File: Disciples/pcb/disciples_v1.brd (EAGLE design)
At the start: 19 x 108.4 mm, 101 parts, among them IC1 OPA1641, IC2 LM324PW, IC3 LM324PW, IC4 TL072D, IC5 LM324PW, IC6 LM4040B10, J1 PJ301_THONKICONN6, J10 PJ301_THONKICONN6, J11 PJ301_THONKICONN6, J2 PJ301_THONKICONN6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

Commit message: Restructure, fixed LEDs
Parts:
- added LED5: WP710A10GD, led:LED3MM
- added R17: 10k, rcl:R0402
- LED4: value WP-710A10GD -> WP710A10SEC/J3
- moved LED2 200.3 mm to (1.27, -447.0)
- moved R9 200.3 mm to (0.64, -442.3)
- moved R10 191.2 mm to (0.64, -461.3)
- moved LED3 191.1 mm to (1.27, -466.1)
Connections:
- new net N$46: IC5.14, LED2.A
- new net N$48: IC5.13, LED2.K, R9.1
- net COMP: no longer IC5.12
- net GND: now also R17.2
- net LOWPASS: now also IC5.12
- net N$17: now also LED3.K, R10.2; no longer LED2.K, R9.1
- net N$30: now also LED3.A; no longer LED2.A
- net N$37: now also LED5.K, R17.1; no longer IC5.13, LED3.K, R10.2
- net N$38: now also LED5.A; no longer IC5.14, LED3.A
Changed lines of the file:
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@@
 <attribute name="VALUE" x="0.3175" y="-149.86" size="1.27" layer="27"/>
 </element>
-<element name="LED4" library="led" package="LED3MM" value="WP-710A10GD" x="1.5875" y="-187.0075" smashed="yes">
+<element name="LED4" library="led" package="LED3MM" value="WP710A10SEC/J3" x="1.5875" y="-187.0075" smashed="yes">
 <attribute name="NAME" x="3.4925" y="-186.6265" size="1.27" layer="25" ratio="10"/>
 <attribute name="VALUE" x="3.4925" y="-188.6585" size="1.27" layer="27" ratio="10"/>
@@
 <attribute name="VALUE" x="5.08" y="-230.1875" size="1.27" layer="27"/>
 </element>
-<element name="R9" library="rcl" package="R0402" value="20k" x="0.635" y="-241.935" smashed="yes">
-<attribute name="NAME" x="0" y="-241.3" size="1.27" layer="25"/>
-<attribute name="VALUE" x="0" y="-243.84" size="1.27" layer="27"/>
-</element>
-<element name="LED2" library="led" package="LED3MM" value="AOL-3MWY4" x="1.27" y="-246.6975" smashed="yes">
-<attribute name="NAME" x="3.175" y="-246.3165" size="1.27" layer="25" ratio="10"/>
-<attribute name="VALUE" x="3.175" y="-248.3485" size="1.27" layer="27" ratio="10"/>
-</element>
-<element name="LED3" library="led" package="LED3MM" value="WP710A10SEC/J4" x="1.27" y="-274.955" smashed="yes">
-<attribute name="NAME" x="3.175" y="-274.574" size="1.27" layer="25" ratio="10"/>
-<attribute name="VALUE" x="3.175" y="-276.606" size="1.27" layer="27" ratio="10"/>
-</element>
-<element name="R10" library="rcl" package="R0402" value="10k" x="5.3975" y="-270.1925" smashed="yes">
-<attribute name="NAME" x="4.7625" y="-269.5575" size="1.27" layer="25"/>
-<attribute name="VALUE" x="4.7625" y="-272.0975" size="1.27" layer="27"/>
-</element>
 <element name="C1" library="rcl" package="C1206" value="22u" x="1.905" y="-280.3525" smashed="yes">
 <attribute name="NAME" x="0.635" y="-279.0825" size="1.27" layer="25"/>
@@
 <attribute name="NAME" x="0" y="-436.5625" size="1.27" layer="25"/>
 <attribute name="VALUE" x="0" y="-439.1025" size="1.27" layer="27"/>
+</element>
+<element name="R9" library="rcl" package="R0402" value="20k" x="0.635" y="-442.2775" smashed="yes">
+<attribute name="NAME" x="0" y="-441.6425" size="1.27" layer="25"/>
+<attribute name="VALUE" x="0" y="-444.1825" size="1.27" layer="27"/>
+</element>
+<element name="LED2" library="led" package="LED3MM" value="AOL-3MWY4" x="1.27" y="-447.04" smashed="yes">
+<attribute name="NAME" x="3.175" y="-446.659" size="1.27" layer="25" ratio="10"/>
+<attribute name="VALUE" x="3.175" y="-448.691" size="1.27" layer="27" ratio="10"/>
+</element>
+<element name="LED3" library="led" package="LED3MM" value="WP710A10SEC/J4" x="1.27" y="-466.09" smashed="yes">
+<attribute name="NAME" x="3.175" y="-465.709" size="1.27" layer="25" ratio="10"/>
+<attribute name="VALUE" x="3.175" y="-467.741" size="1.27" layer="27" ratio="10"/>
+</element>
+<element name="R10" library="rcl" package="R0402" value="10k" x="0.635" y="-461.3275" smashed="yes">
+<attribute name="NAME" x="0" y="-460.6925" size="1.27" layer="25"/>
+<attribute name="VALUE" x="0" y="-463.2325" size="1.27" layer="27"/>
+</element>
+<element name="R17" library="rcl" package="R0402" value="10k" x="0.635" y="-470.8525" smashed="yes">
+<attribute name="NAME" x="0" y="-470.2175" size="1.27" layer="25"/>
+<attribute name="VALUE" x="0" y="-472.7575" size="1.27" layer="27"/>
+</element>
+<element name="LED5" library="led" package="LED3MM" value="WP710A10GD" x="1.27" y="-475.615" smashed="yes">
+<attribute name="NAME" x="3.175" y="-475.234" size="1.27" layer="25" ratio="10"/>
+<attribute name="VALUE" x="3.175" y="-477.266" size="1.27" layer="27" ratio="10"/>
 </element>
 </elements>
@@
 <contactref element="C14" pad="2"/>
 <contactref element="IC6" pad="2"/>
-<contactref element="R9" pad="2"/>
-<contactref element="R10" pad="1"/>
 <contactref element="C1" pad="2"/>
 <contactref element="C2" pad="1"/>
@@
 <contactref element="C20" pad="1"/>
 <contactref element="C21" pad="2"/>
-<wire x1="4.7475" y1="-270.1925" x2="1.285" y2="-241.935" width="0" layer="19" extent="1-1"/>
-<wire x1="3.305" y1="-280.3525" x2="4.7475" y2="-270.1925" width="0" layer="19" extent="1-1"/>
-<wire x1="0.505" y1="-286.7025" x2="3.305" y2="-280.3525" width="0" layer="19" extent="1-1"/>
-<wire x1="1.285" y1="-297.4975" x2="0.505" y2="-286.7025" width="0" layer="19" extent="1-1"/>
-<wire x1="-0.015" y1="-302.5775" x2="1.285" y2="-297.4975" width="0" layer="19" extent="1-1"/>
-<wire x1="3.81" y1="-344.4875" x2="-0.015" y2="-302.5775" width="0" layer="19" extent="1-1"/>
-<wire x1="3.81" y1="-357.505" x2="3.81" y2="-344.4875" width="0" layer="19" extent="1-1"/>
-<wire x1="3.81" y1="-375.6025" x2="3.81" y2="-357.505" width="0" layer="19" extent="1-1"/>
-<wire x1="1.285" y1="-406.7175" x2="3.81" y2="-375.6025" width="0" layer="19" extent="1-1"/>
-<wire x1="-0.015" y1="-411.7975" x2="1.285" y2="-406.7175" width="0" layer="19" extent="1-1"/>
-<wire x1="1.285" y1="-421.9575" x2="-0.015" y2="-411.7975" width="0" layer="19" extent="1-1"/>
-<wire x1="1.8025" y1="-199.39" x2="1.285" y2="-241.935" width="0" layer="19" extent="1-1"/>
+<contactref element="R9" pad="2"/>
+<contactref element="R17" pad="2"/>
+<contactref element="R10" pad="1"/>
+<wire x1="-0.015" y1="-461.3275" x2="1.285" y2="-470.8525" width="0" layer="19" extent="1-1"/>
+<wire x1="1.285" y1="-442.2775" x2="-0.015" y2="-461.3275" width="0" layer="19" extent="1-1"/>
+<wire x1="1.285" y1="-421.9575" x2="1.285" y2="-442.2775" width="0" layer="19" extent="1-1"/>
+<wire x1="-0.015" y1="-411.7975" x2="1.285" y2="-421.9575" width="0" layer="19" extent="1-1"/>
+<wire x1="1.285" y1="-406.7175" x2="-0.015" y2="-411.7975" width="0" layer="19" extent="1-1"/>
+<wire x1="3.81" y1="-375.6025" x2="1.285" y2="-406.7175" width="0" layer="19" extent="1-1"/>
+<wire x1="3.81" y1="-357.505" x2="3.81" y2="-375.6025" width="0" layer="19" extent="1-1"/>
+<wire x1="3.81" y1="-344.4875" x2="3.81" y2="-357.505" width="0" layer="19" extent="1-1"/>
+<wire x1="-0.015" y1="-302.5775" x2="3.81" y2="-344.4875" width="0" layer="19" extent="1-1"/>
+<wire x1="1.285" y1="-297.4975" x2="-0.015" y2="-302.5775" width="0" layer="19" extent="1-1"/>
+<wire x1="0.505" y1="-286.7025" x2="1.285" y2="-297.4975" width="0" layer="19" extent="1-1"/>
+<wire x1="3.305" y1="-280.3525" x2="0.505" y2="-286.7025" width="0" layer="19" extent="1-1"/>
+<wire x1="1.8025" y1="-199.39" x2="3.305" y2="-280.3525" width="0" layer="19" extent="1-1"/>
 <wire x1="2.855" y1="-194.14" x2="1.8025" y2="-199.39" width="0" layer="19" extent="1-1"/>
 <wire x1="7.5175" y1="-182.245" x2="2.855" y2="-194.14" width="0" layer="19" extent="1-1"/>
@@
 <signal name="COMP">
 <contactref element="R33" pad="1"/>
-<contactref element="IC5" pad="12"/>
-<wire x1="9.8275" y1="-108.2675" x2="2.8575" y2="-397.9672" width="0" layer="19" extent="1-1"/>
 </signal>
 <signal name="N$28">
@@
 </signal>
 <signal name="N$30">
-<contactref element="LED2" pad="A"/>
 <contactref element="IC5" pad="1"/>
-<wire x1="1.5875" y1="-403.4028" x2="0" y2="-246.6975" width="0" layer="19" extent="1-1"/>
+<contactref element="LED3" pad="A"/>
+<wire x1="1.5875" y1="-403.4028" x2="0" y2="-466.09" width="0" layer="19" extent="1-1"/>
 </signal>
 <signal name="N$17">
-<contactref element="R9" pad="1"/>
-<contactref element="LED2" pad="K"/>
 <contactref element="IC5" pad="2"/>
-<wire x1="-0.015" y1="-241.935" x2="2.54" y2="-246.6975" width="0" layer="19" extent="1-1"/>
-<wire x1="2.2225" y1="-403.4028" x2="2.54" y2="-246.6975" width="0" layer="19" extent="1-1"/>
-</signal>
-<signal name="N$37">
 <contactref element="LED3" pad="K"/>
 <contactref element="R10" pad="2"/>
-<contactref element="IC5" pad="13"/>
-<wire x1="2.54" y1="-274.955" x2="2.2225" y2="-397.9672" width="0" layer="19" extent="1-1"/>
-<wire x1="6.0475" y1="-270.1925" x2="2.54" y2="-274.955" width="0" layer="19" extent="1-1"/>
-</signal>
-<signal name="N$38">
-<contactref element="LED3" pad="A"/>
-<contactref element="IC5" pad="14"/>
-<wire x1="0" y1="-274.955" x2="1.5875" y2="-397.9672" width="0" layer="19" extent="1-1"/>
+<wire x1="1.285" y1="-461.3275" x2="2.54" y2="-466.09" width="0" layer="19" extent="1-1"/>
+<wire x1="2.2225" y1="-403.4028" x2="1.285" y2="-461.3275" width="0" layer="19" extent="1-1"/>
 </signal>
 <signal name="N$27">
@@
 <contactref element="IC5" pad="9"/>
 <contactref element="IC5" pad="8"/>
+<contactref element="IC5" pad="12"/>
 <wire x1="5.3975" y1="-397.9672" x2="4.7625" y2="-397.9672" width="0" layer="19" extent="1-1"/>
+<wire x1="2.8575" y1="-397.9672" x2="4.7625" y2="-397.9672" width="0" layer="19" extent="1-1"/>
 <wire x1="3.81" y1="-373.0625" x2="4.7625" y2="-397.9672" width="0" layer="19" extent="1-1"/>
 <wire x1="-0.015" y1="-361.315" x2="3.81" y2="-373.0625" width="0" layer="19" extent="1-1"/>
@@
 <contactref element="R16" pad="2"/>
 </signal>
+<signal name="N$46">
+<contactref element="IC5" pad="14"/>
+<contactref element="LED2" pad="A"/>
+<wire x1="1.5875" y1="-397.9672" x2="0" y2="-447.04" width="0" layer="19" extent="1-1"/>
+</signal>
+<signal name="N$48">
+<contactref element="IC5" pad="13"/>
+<contactref element="LED2" pad="K"/>
+<contactref element="R9" pad="1"/>
+<wire x1="-0.015" y1="-442.2775" x2="2.54" y2="-447.04" width="0" layer="19" extent="1-1"/>
+<wire x1="2.2225" y1="-397.9672" x2="-0.015" y2="-442.2775" width="0" layer="19" extent="1-1"/>
+</signal>
+<signal name="N$37">
+<contactref element="R17" pad="1"/>
+<contactref element="LED5" pad="K"/>
+<wire x1="-0.015" y1="-470.8525" x2="2.54" y2="-475.615" width="0" layer="19" extent="1-1"/>
+</signal>
+<signal name="N$38">
+<contactref element="LED5" pad="A"/>
+</signal>
 </signals>

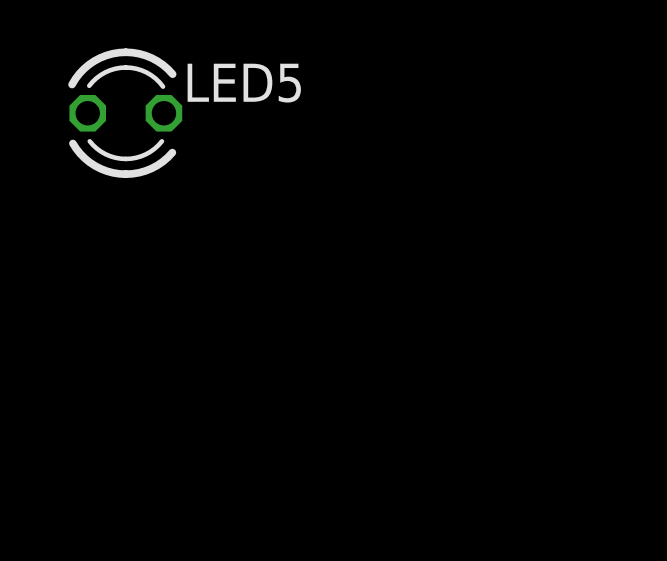
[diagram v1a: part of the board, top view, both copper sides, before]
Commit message: More labels, voltage reference
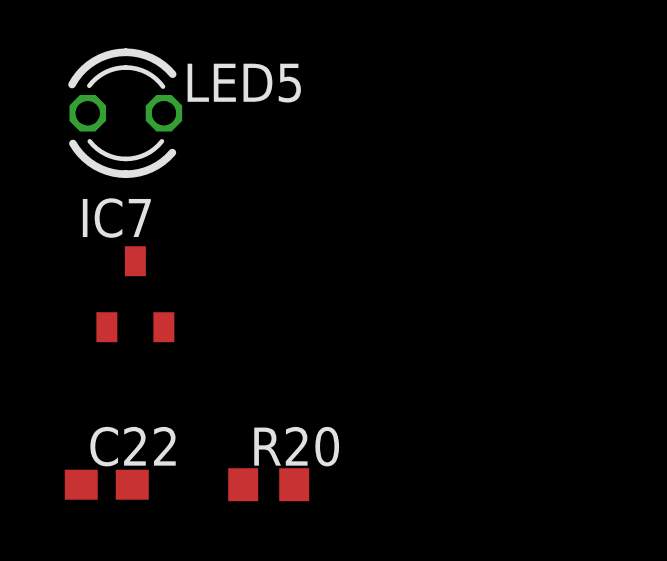
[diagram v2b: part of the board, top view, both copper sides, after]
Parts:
- added C22: 100n, rcl:C0603
- added IC7: LM4040B50, texas:DBZ_R-PDSO-G3
- added R20: 3.3k, rcl:R0603
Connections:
- new net AREF_+5: C22.1, IC7.1, R20.2
- net GND: now also C22.2, IC7.2
- net VCC: now also R20.1
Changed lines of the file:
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@@
 <attribute name="VALUE" x="3.175" y="-477.266" size="1.27" layer="27" ratio="10"/>
+</element>
+<element name="IC7" library="texas" package="DBZ_R-PDSO-G3" value="LM4040B50" x="1.5875" y="-481.6475" smashed="yes">
+<attribute name="NAME" x="-0.3175" y="-479.7425" size="1.27" layer="25"/>
+<attribute name="VALUE" x="-0.3175" y="-484.8225" size="1.27" layer="27"/>
+</element>
+<element name="R20" library="rcl" package="R0603" value="3.3k" x="6.0325" y="-487.9975" smashed="yes">
+<attribute name="NAME" x="5.3975" y="-487.3625" size="1.27" layer="25"/>
+<attribute name="VALUE" x="5.3975" y="-489.9025" size="1.27" layer="27"/>
+</element>
+<element name="C22" library="rcl" package="C0603" value="100n" x="0.635" y="-487.9975" smashed="yes">
+<attribute name="NAME" x="0" y="-487.3625" size="1.27" layer="25"/>
+<attribute name="VALUE" x="0" y="-489.9025" size="1.27" layer="27"/>
 </element>
 </elements>
@@
 <contactref element="R17" pad="2"/>
 <contactref element="R10" pad="1"/>
+<contactref element="IC7" pad="2"/>
+<contactref element="C22" pad="2"/>
+<wire x1="2.5375" y1="-482.7475" x2="1.485" y2="-487.9975" width="0" layer="19" extent="1-1"/>
+<wire x1="1.285" y1="-470.8525" x2="2.5375" y2="-482.7475" width="0" layer="19" extent="1-1"/>
 <wire x1="-0.015" y1="-461.3275" x2="1.285" y2="-470.8525" width="0" layer="19" extent="1-1"/>
 <wire x1="1.285" y1="-442.2775" x2="-0.015" y2="-461.3275" width="0" layer="19" extent="1-1"/>
@@
 <contactref element="IC5" pad="4"/>
 <contactref element="C19" pad="1"/>
+<contactref element="R20" pad="1"/>
+<wire x1="-0.015" y1="-406.7175" x2="5.1825" y2="-487.9975" width="0" layer="19" extent="1-1"/>
+<wire x1="3.4925" y1="-403.4028" x2="-0.015" y2="-406.7175" width="0" layer="19" extent="1-1"/>
+<wire x1="-0.015" y1="-297.4975" x2="3.4925" y2="-403.4028" width="0" layer="19" extent="1-1"/>
+<wire x1="0.505" y1="-280.3525" x2="-0.015" y2="-297.4975" width="0" layer="19" extent="1-1"/>
+<wire x1="5.5" y1="-199.39" x2="0.505" y2="-280.3525" width="0" layer="19" extent="1-1"/>
 <wire x1="11.215" y1="-182.245" x2="5.5" y2="-199.39" width="0" layer="19" extent="1-1"/>
 <wire x1="7.5175" y1="-172.085" x2="11.215" y2="-182.245" width="0" layer="19" extent="1-1"/>
 <wire x1="13.7975" y1="-159.385" x2="7.5175" y2="-172.085" width="0" layer="19" extent="1-1"/>
 <wire x1="1.905" y1="-157.42" x2="13.7975" y2="-159.385" width="0" layer="19" extent="1-1"/>
-<wire x1="0.505" y1="-280.3525" x2="5.5" y2="-199.39" width="0" layer="19" extent="1-1"/>
-<wire x1="-0.015" y1="-297.4975" x2="0.505" y2="-280.3525" width="0" layer="19" extent="1-1"/>
-<wire x1="3.4925" y1="-403.4028" x2="-0.015" y2="-297.4975" width="0" layer="19" extent="1-1"/>
-<wire x1="-0.015" y1="-406.7175" x2="3.4925" y2="-403.4028" width="0" layer="19" extent="1-1"/>
 <wire x1="6.8072" y1="12.065" x2="1.905" y2="-157.42" width="0" layer="19" extent="1-1"/>
 <wire x1="5.3975" y1="13.32" x2="6.8072" y2="12.065" width="0" layer="19" extent="1-1"/>
@@
 <contactref element="LED5" pad="A"/>
 </signal>
+<signal name="AREF_+5">
+<contactref element="IC7" pad="1"/>
+<contactref element="R20" pad="2"/>
+<contactref element="C22" pad="1"/>
+<wire x1="0.6375" y1="-482.7475" x2="-0.215" y2="-487.9975" width="0" layer="19" extent="1-1"/>
+<wire x1="6.8825" y1="-487.9975" x2="-0.215" y2="-487.9975" width="0" layer="19" extent="1-1"/>
+</signal>
 </signals>
